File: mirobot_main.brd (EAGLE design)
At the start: 100 x 40.6 mm, 25 parts, among them IC1 ULN2003AN, IC2 ULN2003AN, IC3 MEGA8-P, IC4 5V, IC5 3.3V, Q2 16M

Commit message: Version 1.1 of the PCB
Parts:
- removed JP2: Stepper1, pinhead:1X05
- removed JP3: Stepper2, pinhead:1X05
- removed JP7: RF, pinhead:1X04
- removed LED14: POWER LED, led:LED3MM
- added COMMS: (no value), pinhead:1X04
- added EXPANSION: (no value), pinhead:1X13
- added POWER: (no value), led:LED3MM
- added X1, X2: 22-23-2051, con-molex:22-23-2051
- C5, C8: device rcl:E3,5-8 -> rcl:E2-5
- IC3: value MEGA8-P -> ATMEGA 328
- JP6: value Batt -> Battery
- moved IC3 36.3 mm to (54.9, 30.0)
- moved Q2 36.0 mm to (59.9, 21.1)
- moved C4 36.0 mm to (28.4, 24.4)
- moved JP6 35.7 mm to (21.9, 20.4)
- moved JP4 33.0 mm to (46.0, 41.9), turned to 180 degrees
- moved JP1 33.0 mm to (39.6, 20.4)
- moved C1 32.3 mm to (67.5, 21.0), turned to 90 degrees
- moved R11 32.2 mm to (34.3, 26.2), turned to 90 degrees
- moved C2 31.9 mm to (52.5, 21.0), turned to 90 degrees
- moved C8 29.0 mm to (15.7, 32.8)
- moved JP5 27.3 mm to (30.0, 33.0)
- moved IC2 26.8 mm to (68.8, 45.2)
- moved C5 25.9 mm to (21.3, 32.8)
- moved IC1 23.3 mm to (24.9, 45.5)
- moved S1 22.3 mm to (14.0, 25.1), turned to 180 degrees
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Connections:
- new net PB0: EXPANSION.3, IC3.14
- new net PB2: EXPANSION.4, IC3.16
- new net PB3: EXPANSION.5, IC3.17
- new net PB4: EXPANSION.6, IC3.18
- new net PB5: EXPANSION.7, IC3.19
- new net PC4: EXPANSION.8, IC3.27
- new net PC5: EXPANSION.9, IC3.28
- new net PD2: EXPANSION.10, IC3.4
- new net PD3: EXPANSION.11, IC3.5
- net +3V3: now also COMMS.1, EXPANSION.1; no longer JP7.1
- net +5V: now also EXPANSION.13, R4.2
- net GND: now also COMMS.4, EXPANSION.12, EXPANSION.2, POWER.K; no longer JP7.4, LED14.K
- net N$1: now also X1.1; no longer JP2.1
- net N$10: now also X2.3; no longer JP3.3
- net N$11: now also X2.4; no longer JP3.4
- net N$19: now also COMMS.2; no longer JP7.2
- net N$2: now also X1.2; no longer JP2.2
- net N$20: now also POWER.A; no longer LED14.A
- net N$3: now also X1.3; no longer JP2.3
- net N$4: now also X1.4; no longer JP2.4
- net N$8: now also X2.1; no longer JP3.1
- net N$9: now also X2.2; no longer JP3.2
- net RXD: now also COMMS.3; no longer JP7.3
- net SERVO: now also IC3.15; no longer IC3.5
- net V+: now also X1.5, X2.5; no longer JP2.5, JP3.5
- net VCC: no longer R4.2
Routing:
- net V+: track 183.0 -> 137.2 mm
- net PC5: track 0.00 -> 33.0 mm
- net PC4: track 0.00 -> 21.0 mm
- net +5V: track 53.1 -> 73.9 mm
- net RXD: track 70.4 -> 50.3 mm
- net PD3: track 0.00 -> 19.9 mm
- net EXT_RESET: track 21.8 -> 4.87 mm
- net SERVO: track 13.5 -> 28.5 mm
- net PB0: track 0.00 -> 14.6 mm
- net VCC: track 28.3 -> 13.8 mm
- net TXD: track 52.0 -> 66.1 mm
- net PD2: track 0.00 -> 13.5 mm
- net N$12: track 33.1 -> 20.6 mm
- net +3V3: track 9.20 -> 19.8 mm
- net N$17: track 24.0 -> 15.8 mm
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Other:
- board size 100 x 40.6 mm -> 77.2 x 42.5 mm
- board text added: "+"
- board text added: "-"
- board text added: "BATT"
- board text added: "BLACK"
- board text added: "BROWN"
- board text added: "Ben Pirt 2013"
- board text added: "GREEN"
- board text added: "Mirobot v1.1"
- board text added: "USB"
- board text added: "YELLOW"

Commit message: Version 1.2 of the Mirobot PCB
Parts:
- removed IC4: 5V, v-reg:78LXX
- added 5V: (no value), v-reg:78MXXS
- moved X2 14.4 mm to (79.0, 44.7), turned to 90 degrees
- moved X1 11.5 mm to (14.5, 44.7), turned to 270 degrees
- moved R4 7.66 mm to (22.9, 37.6)
- moved IC2 6.86 mm to (62.0, 45.5)
- moved IC1 4.83 mm to (29.7, 45.5)
- moved JP6 4.83 mm to (26.7, 20.4)
- moved JP4 3.30 mm to (46.0, 45.2), turned to 90 degrees
- moved POWER 2.59 mm to (11.4, 32.8)
- moved S1 1.48 mm to (13.2, 23.9), turned to 270 degrees
- moved JP1 1.30 mm to (40.9, 20.6)
- moved COMMS 1.02 mm to (75.9, 20.6)
- moved C8 1.02 mm to (16.8, 32.8)
- moved C5 0.76 mm to (22.1, 32.8)
- renumbered IC5 to 3.3V
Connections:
- net GND: now also 5V.GND; no longer IC4.GND
- net V+: now also 5V.IN; no longer IC4.IN
- net VCC: now also 5V.OUT; no longer IC4.OUT
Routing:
- net N$8: track 5.92 -> 31.4 mm
- net N$9: track 5.92 -> 27.8 mm
- net N$10: track 5.92 -> 23.5 mm
- net N$11: track 5.92 -> 19.8 mm
- net N$4: track 4.83 -> 17.2 mm
- net N$3: track 4.83 -> 13.8 mm
- net N$20: track 2.51 -> 10.4 mm
- net SERVO: track 28.5 -> 34.7 mm
- net N$5: track 25.9 -> 19.6 mm
- net N$13: track 43.6 -> 37.8 mm
- net N$14: track 37.8 -> 32.4 mm
- net N$2: track 4.83 -> 10.0 mm
- net N$15: track 32.5 -> 27.7 mm
- net VCC: track 13.8 -> 18.6 mm
- net N$16: track 15.8 -> 20.1 mm
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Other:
- board size 77.2 x 42.5 mm -> 73.9 x 39.9 mm
- board text added: "Mirobot v1.2"
- board text removed: "Mirobot v1.1"

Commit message: Version 1.3 of the Mirobot PCB
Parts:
- removed COMMS: (no value), pinhead:1X04
- removed JP1: USB, pinhead:1X06
- removed JP4: Servo, pinhead:1X03
- removed POWER: (no value), led:LED3MM
- added SERVO: (no value), SparkFun-Connectors:1X03_LOCK_LONGPADS
- added STATUS: (no value), Child-Friendly-Parts:LED3MM
- added USB: (no value), SparkFun-Connectors:1X06_LOCK_LONGPADS
- added WIFI: (no value), Child-Friendly-Parts:2X03
- 3.3V: device v-reg:78LXX -> Child-Friendly-Parts:78LXX
- C1, C2: device rcl:C025-024X044 -> Child-Friendly-Parts:C025-024X044
- C4, C7: device rcl:C050-025X075 -> Child-Friendly-Parts:C050-025X075
- C5, C8: device rcl:E2-5 -> Child-Friendly-Parts:E2-5
- EXPANSION: device pinhead:1X13 -> pinhead:1X10
- JP5: device pinhead:2X03 -> Child-Friendly-Parts:2X03
- Q2: device crystal:HC49/S -> Child-Friendly-Parts:HC49/S
- R1, R11, R2, R4: device rcl:0204/5 -> Child-Friendly-Parts:0204/5
- moved R11 16.6 mm to (17.8, 24.4)
- moved R4 11.7 mm to (34.0, 34.3), turned to 270 degrees
- moved 3.3V 8.58 mm to (78.5, 23.7), turned to 180 degrees
- moved R2 8.32 mm to (72.9, 21.8), turned to 0 degrees
- moved R1 7.89 mm to (72.9, 19.6), turned to 0 degrees
- moved JP5 6.18 mm to (23.9, 34.0)
- moved C5 5.18 mm to (17.0, 33.8)
- moved C8 4.93 mm to (11.9, 33.8)
- moved X2 1.78 mm to (77.2, 44.7)
- moved 5V 1.52 mm to (24.1, 23.9)
- moved EXPANSION 1.27 mm to (59.9, 37.6)
- moved JP6 1.05 mm to (27.6, 19.9), turned to 0 degrees
- moved C1 0.41 mm to (67.1, 21.1)
- moved C2 0.33 mm to (52.8, 21.1)
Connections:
- removed net PB0: EXPANSION.3, IC3.14
- removed net PC4: EXPANSION.8, IC3.27
- removed net PC5: EXPANSION.9, IC3.28
- new net NREADY: IC3.28, WIFI.5
- new net STATUS: IC3.14, R4.2
- new net WIFI_RESET: IC3.27, WIFI.6
- net +3V3: now also WIFI.2; no longer COMMS.1
- net +5V: now also EXPANSION.10, SERVO.2; no longer EXPANSION.13, JP4.2, R4.2
- net EXT_RESET: now also USB.1; no longer JP1.1
- net GND: now also EXPANSION.9, SERVO.3, STATUS.K, USB.6, WIFI.1; no longer COMMS.4, EXPANSION.12, JP1.6, JP4.3, POWER.K
- net N$19: now also WIFI.3; no longer COMMS.2
- net N$20: now also STATUS.A; no longer POWER.A
- net PB2: now also EXPANSION.3; no longer EXPANSION.4
- net PB3: now also EXPANSION.4; no longer EXPANSION.5
- net PB4: now also EXPANSION.5; no longer EXPANSION.6
- net PB5: now also EXPANSION.6; no longer EXPANSION.7
- net PD2: now also EXPANSION.7; no longer EXPANSION.10
- net PD3: now also EXPANSION.8; no longer EXPANSION.11
- net RXD: now also USB.3, WIFI.4; no longer COMMS.3, JP1.3
- net SERVO: now also SERVO.1; no longer JP4.1
- net TXD: now also USB.2; no longer JP1.2
- net USBVCC: now also USB.4; no longer JP1.4
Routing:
- net NREADY: track 0.00 -> 43.3 mm
- net STATUS: track 0.00 -> 40.5 mm
- net WIFI_RESET: track 0.00 -> 37.8 mm
- net PC5: track 33.0 -> 0.00 mm
- net +5V: track 71.6 -> 100.3 mm
- net V+: track 137.0 -> 159.4 mm, vias 1 -> 2
- net PC4: track 21.0 -> 0.00 mm
- net PB0: track 14.6 -> 0.00 mm
- net TXD: track 62.0 -> 49.7 mm
- net RXD: track 46.9 -> 57.0 mm
- net PD2: track 13.5 -> 23.5 mm
- net PD3: track 19.9 -> 13.5 mm
- net USBVCC: track 19.6 -> 25.5 mm, vias 0 -> 1
- net N$20: track 10.4 -> 4.57 mm
- net VSS: track 11.5 -> 14.8 mm
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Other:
- board text added: "Ben Pirt 2014"
- board text added: "Mirobot v1.3"
- board text removed: "Ben Pirt 2013"
- board text removed: "Mirobot v1.2"

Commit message: Version 1.4 of the mian PCB and 1.1 of the WiFi PCB
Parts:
- JP6: device pinhead:1X02 -> Child-Friendly-Parts:1X02
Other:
- board text added: "Mirobot v1.4"
- board text removed: "Mirobot v1.3"
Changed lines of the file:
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@@
 <text x="27.559" y="29.972" size="1.016" layer="25" rot="R180">USB</text>
 <text x="23.114" y="29.972" size="1.016" layer="25" rot="R180">BATT</text>
-<text x="27.94" y="53.594" size="1.27" layer="25" rot="R180">Mirobot v1.3</text>
+<text x="27.94" y="53.594" size="1.27" layer="25" rot="R180">Mirobot v1.4</text>
 <text x="47.244" y="53.594" size="1.27" layer="25" rot="R180">Ben Pirt 2014</text>
 <text x="49.911" y="18.288" size="0.8128" layer="25" rot="R90">BLACK</text>
@@
 <attribute name="VALUE" x="32.385" y="23.368" size="0.6096" layer="27" ratio="10"/>
 </element>
-<element name="JP6" library="pinhead" package="1X02" value="Battery" x="27.635" y="19.936" smashed="yes">
+<element name="JP6" library="Child-Friendly-Parts" package="1X02" value="Battery" x="27.635" y="19.936" smashed="yes">
 <attribute name="VALUE" x="25.4" y="21.717" size="1.016" layer="27"/>
 </element>
@@
 <wire x1="21.336" y1="30.988" x2="23.876" y2="28.448" width="0.8128" layer="1"/>
 <wire x1="23.876" y1="28.448" x2="23.876" y2="22.425" width="0.8128" layer="1"/>
-<wire x1="23.876" y1="22.425" x2="26.365" y2="19.936" width="0.8128" layer="1"/>
+<wire x1="23.876" y1="22.425" x2="26.492" y2="19.936" width="0.8128" layer="1"/>
 </signal>
 <signal name="N$19">

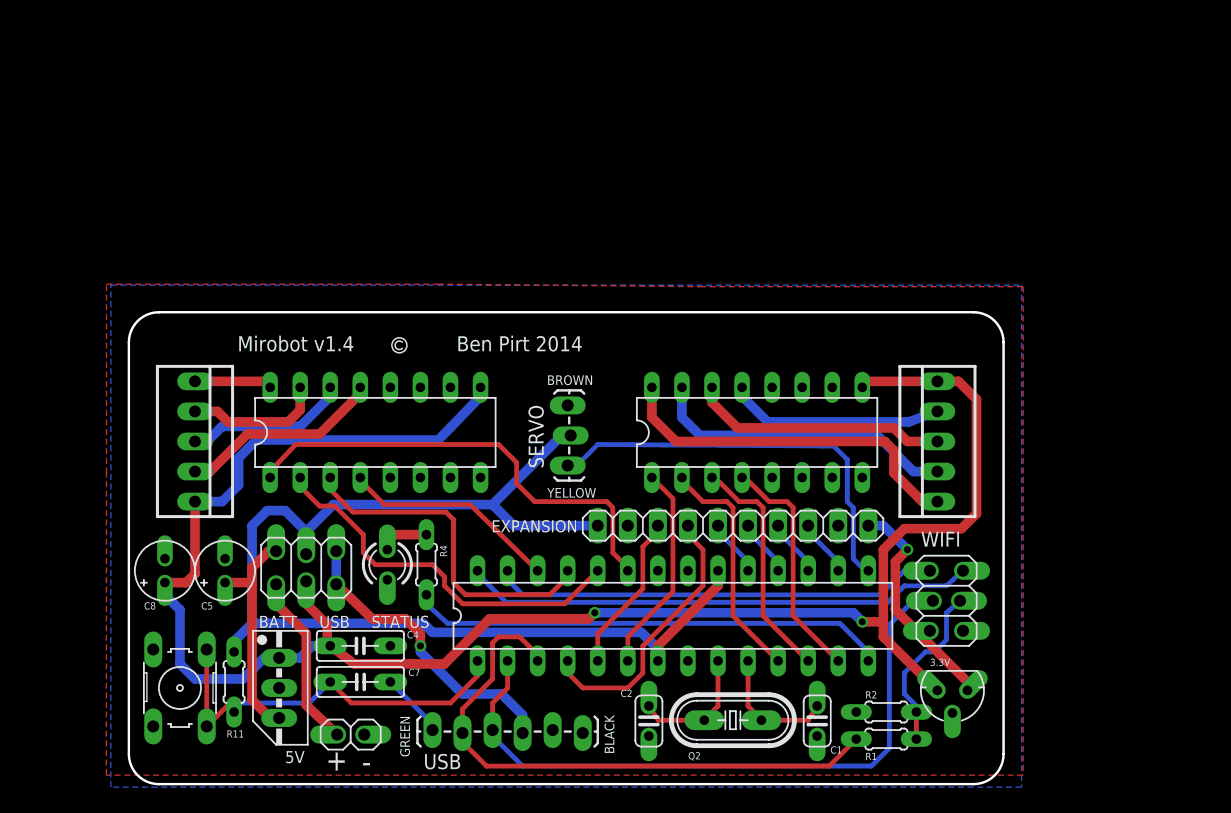
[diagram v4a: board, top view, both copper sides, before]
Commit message: Modified board to use the -T WiFi module
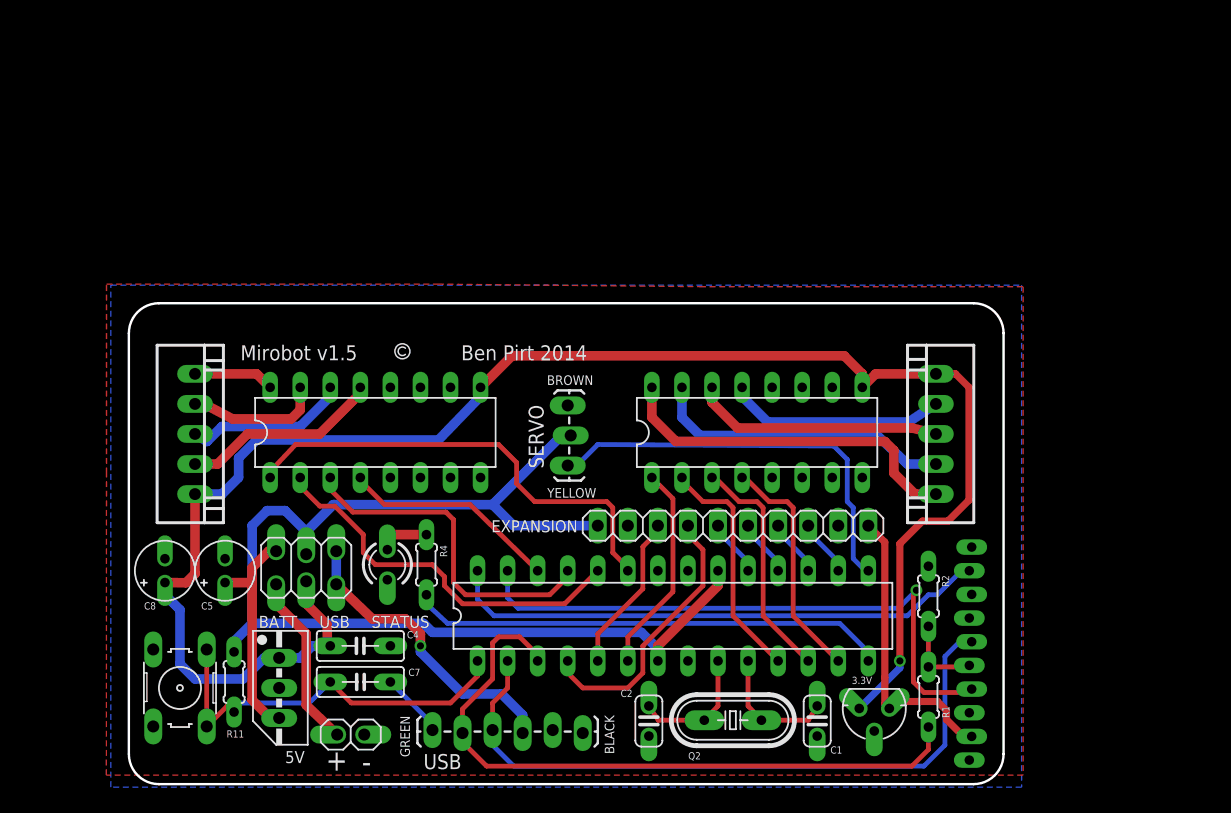
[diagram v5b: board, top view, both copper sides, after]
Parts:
- removed WIFI: (no value), Child-Friendly-Parts:2X03
- added U$1: USR_WIFI-T, usr_wifi:WIFI_MODULE-T
- X1, X2: value 22-23-2051 -> 5_PIN_STEPPER; device con-molex:22-23-2051 -> custom:5_PIN_STEPPER
- moved R2 10.4 mm to (76.5, 31.6), turned to 270 degrees
- moved 3.3V 6.78 mm to (71.9, 22.1)
- moved R1 5.03 mm to (76.5, 23.1), turned to 90 degrees
- moved X2 0.65 mm to (77.1, 45.3)
- moved X1 0.63 mm to (14.5, 45.3)
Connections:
- net +3V3: now also U$1.+3V3; no longer WIFI.2
- net GND: now also U$1.GND; no longer WIFI.1
- net N$19: now also U$1.RX; no longer WIFI.3
- net NREADY: now also U$1.PWM_2; no longer WIFI.5
- net RXD: now also U$1.TX; no longer WIFI.4
- net WIFI_RESET: now also U$1.EXT_RESET; no longer WIFI.6
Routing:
- net V+: track 159.4 -> 144.3 mm, vias 2 -> 1
- net WIFI_RESET: track 37.8 -> 51.1 mm, vias 0 -> 1
- net N$19: track 14.7 -> 6.94 mm
- net TXD: track 49.7 -> 57.3 mm
- net +3V3: track 20.1 -> 25.0 mm, vias 1 -> 0
- net NREADY: track 43.3 -> 46.1 mm
- net RXD: track 57.0 -> 57.6 mm
- net N$10: track 21.7 -> 21.1 mm
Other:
- board size 73.9 x 39.9 mm -> 73.9 x 40.6 mm
- board text added: "Mirobot v1.5"
- board text removed: "Mirobot v1.4"

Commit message: Rotated the WiFi module so that it doesn't hit the other components
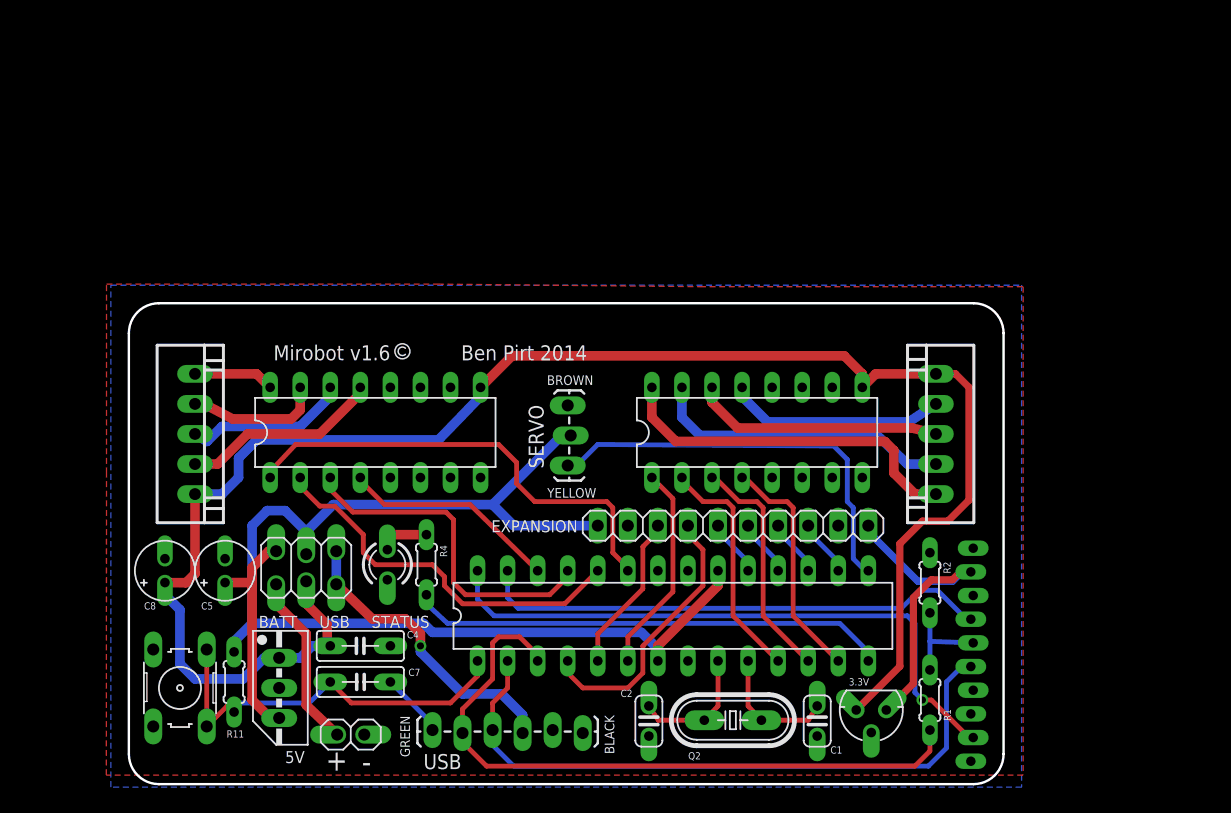
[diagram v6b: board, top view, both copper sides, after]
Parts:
- moved U$1 1.91 mm to (80.1, 27.7), turned to 270 degrees
- moved R2 1.15 mm to (76.6, 32.8)
- moved 3.3V 0.28 mm to (71.6, 22.0)
- moved R1 0.28 mm to (76.6, 22.9)
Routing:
- net WIFI_RESET: track 51.1 -> 43.5 mm, vias 1 -> 0
- net NREADY: track 46.1 -> 52.6 mm, vias 0 -> 1
- net +3V3: track 25.0 -> 27.7 mm
- net RXD: track 57.6 -> 55.7 mm
- net N$19: track 6.94 -> 8.48 mm
- net V+: track 144.3 -> 144.6 mm, vias 1 -> 0
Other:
- board text added: "Mirobot v1.6"
- board text removed: "Mirobot v1.5"
